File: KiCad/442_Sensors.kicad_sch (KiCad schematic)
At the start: 9 parts, among them U4 MS560702BA03-50, U5 BMI088, U6 SAM-M10Q

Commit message: fixed a couple issues
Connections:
- net +3V3: no longer U4.4 (~{CSB})
- net GND: now also U4.4 (~{CSB})
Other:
- moved on the sheet: C20
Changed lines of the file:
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@@
+	)
+	(junction
+		(at 88.9 99.06)
+		(diameter 0)
+		(color 0 0 0 0)
 	)
 	(junction
@@
 	(wire
 		(pts
-			(xy 133.35 96.52) (xy 137.16 96.52)
+			(xy 133.35 97.79) (xy 133.35 96.52)
 		)
 		(stroke
@@
 	(wire
 		(pts
-			(xy 77.47 96.52) (xy 91.44 96.52)
-		)
-		(stroke
-			(width 0)
-			(type default)
-		)
-	)
-	(wire
-		(pts
 			(xy 194.31 81.28) (xy 200.66 81.28)
 		)
@@
 	(wire
 		(pts
-			(xy 80.01 99.06) (xy 91.44 99.06)
+			(xy 88.9 99.06) (xy 91.44 99.06)
+		)
+		(stroke
+			(width 0)
+			(type default)
+		)
+	)
+	(wire
+		(pts
+			(xy 80.01 99.06) (xy 88.9 99.06)
 		)
 		(stroke
@@
 	(wire
 		(pts
+			(xy 88.9 96.52) (xy 88.9 99.06)
+		)
+		(stroke
+			(width 0)
+			(type default)
+		)
+	)
+	(wire
+		(pts
 			(xy 113.03 46.99) (xy 95.25 46.99)
 		)
@@
 	(wire
 		(pts
+			(xy 91.44 96.52) (xy 88.9 96.52)
+		)
+		(stroke
+			(width 0)
+			(type default)
+		)
+	)
+	(wire
+		(pts
 			(xy 194.31 78.74) (xy 200.66 78.74)
 		)
@@
 		(pts
 			(xy 121.92 106.68) (xy 123.19 106.68)
+		)
+		(stroke
+			(width 0)
+			(type default)
+		)
+	)
+	(wire
+		(pts
+			(xy 133.35 95.25) (xy 133.35 96.52)
 		)
 		(stroke
@@
 	(symbol
 		(lib_id "power:GND")
-		(at 133.35 101.6 0)
+		(at 133.35 102.87 0)
 		(unit 1)
 		(exclude_from_sim no)
@@
 		(fields_autoplaced yes)
 		(property "Reference" "#PWR051"
+			(at 133.35 109.22 0)
+			(effects
+				(font
+					(size 1.27 1.27)
+				)
+				(hide yes)
+			)
+		)
+		(property "Value" "GND"
 			(at 133.35 107.95 0)
 			(effects
@@
 					(size 1.27 1.27)
 				)
-				(hide yes)
-			)
-		)
-		(property "Value" "GND"
-			(at 133.35 106.68 0)
-			(effects
-				(font
-					(size 1.27 1.27)
-				)
 			)
 		)
 		(property "Footprint" ""
-			(at 133.35 101.6 0)
+			(at 133.35 102.87 0)
 			(effects
 				(font
@@
 		)
 		(property "Datasheet" ""
-			(at 133.35 101.6 0)
+			(at 133.35 102.87 0)
 			(effects
 				(font
@@
 		)
 		(property "Description" "Power symbol creates a global label with name \"GND\" , ground"
-			(at 133.35 101.6 0)
+			(at 133.35 102.87 0)
 			(effects
 				(font
@@
 	(symbol
 		(lib_id "power:+3V3")
-		(at 137.16 96.52 270)
+		(at 133.35 95.25 0)
 		(unit 1)
 		(exclude_from_sim no)
@@
 		(fields_autoplaced yes)
 		(property "Reference" "#PWR063"
-			(at 133.35 96.52 0)
+			(at 133.35 99.06 0)
 			(effects
 				(font
@@
 		)
 		(property "Value" "+3V3"
-			(at 140.97 96.5199 90)
+			(at 135.89 93.9799 0)
 			(effects
 				(font
@@
 		)
 		(property "Footprint" ""
-			(at 137.16 96.52 0)
+			(at 133.35 95.25 0)
 			(effects
 				(font
@@
 		)
 		(property "Datasheet" ""
-			(at 137.16 96.52 0)
+			(at 133.35 95.25 0)
 			(effects
 				(font
@@
 		)
 		(property "Description" "Power symbol creates a global label with name \"+3V3\""
-			(at 137.16 96.52 0)
+			(at 133.35 95.25 0)
 			(effects
 				(font
@@
 	(symbol
 		(lib_id "power:+3V3")
-		(at 77.47 96.52 90)
-		(unit 1)
-		(exclude_from_sim no)
-		(in_bom yes)
-		(on_board yes)
-		(dnp no)
-		(fields_autoplaced yes)
-		(property "Reference" "#PWR064"
-			(at 81.28 96.52 0)
-			(effects
-				(font
-					(size 1.27 1.27)
-				)
-				(hide yes)
-			)
-		)
-		(property "Value" "+3V3"
-			(at 73.66 96.5199 90)
-			(effects
-				(font
-					(size 1.27 1.27)
-				)
-				(justify left)
-			)
-		)
-		(property "Footprint" ""
-			(at 77.47 96.52 0)
-			(effects
-				(font
-					(size 1.27 1.27)
-				)
-				(hide yes)
-			)
-		)
-		(property "Datasheet" ""
-			(at 77.47 96.52 0)
-			(effects
-				(font
-					(size 1.27 1.27)
-				)
-				(hide yes)
-			)
-		)
-		(property "Description" "Power symbol creates a global label with name \"+3V3\""
-			(at 77.47 96.52 0)
-			(effects
-				(font
-					(size 1.27 1.27)
-				)
-				(hide yes)
-			)
-		)
-		(pin "1"
-		)
-		(instances
-			(project "Senior Project"
-				(path "/16f8cce7-467e-4342-b55a-00af81cd6f69/c3ab4c5a-4cab-469f-8c3a-b4c939a78ff3"
-					(reference "#PWR064")
-					(unit 1)
-				)
-			)
-		)
-	)
-	(symbol
-		(lib_id "power:+3V3")
 		(at 113.03 46.99 0)
 		(unit 1)
@@
 	(symbol
 		(lib_id "Device:C_Small")
-		(at 133.35 99.06 0)
+		(at 133.35 100.33 0)
 		(unit 1)
 		(exclude_from_sim no)
@@
 		(fields_autoplaced yes)
 		(property "Reference" "C20"
-			(at 135.89 97.7962 0)
+			(at 135.89 99.0662 0)
 			(effects
 				(font
@@
 		)
 		(property "Value" "100nF"
-			(at 135.89 100.3362 0)
+			(at 135.89 101.6062 0)
 			(effects
 				(font
@@
 		)
 		(property "Footprint" "Capacitor_SMD:C_0402_1005Metric"
-			(at 133.35 99.06 0)
+			(at 133.35 100.33 0)
 			(effects
 				(font
@@
 		)
 		(property "Datasheet" "~"
-			(at 133.35 99.06 0)
+			(at 133.35 100.33 0)
 			(effects
 				(font
@@
 		)
 		(property "Description" "Unpolarized capacitor, small symbol"
-			(at 133.35 99.06 0)
+			(at 133.35 100.33 0)
 			(effects
 				(font
@@
 		)
 		(property "LCSC" "C1525"
-			(at 133.35 99.06 0)
-			(effects
-				(font
+			(at 133.35 100.33 0)
+			(effects
+				(font

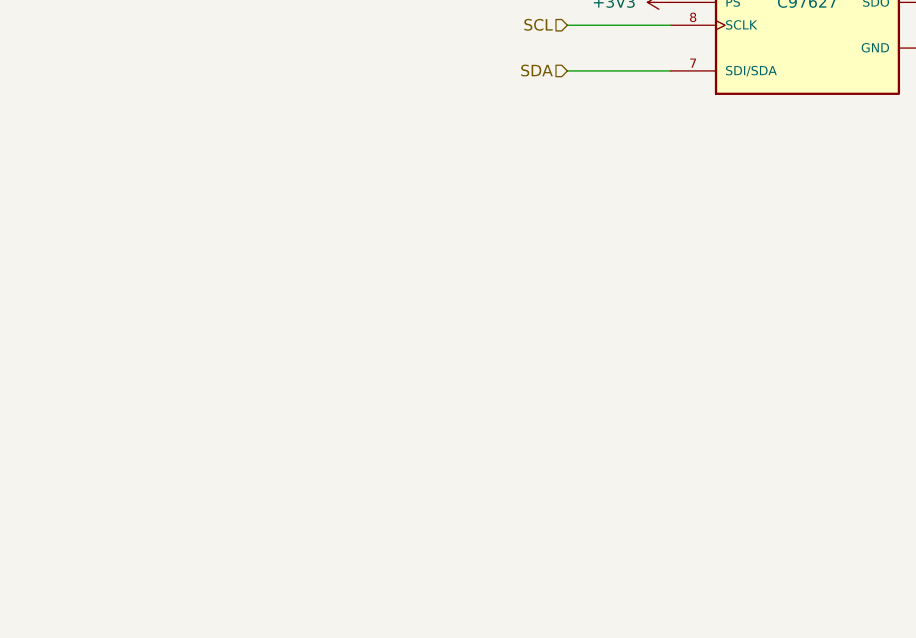
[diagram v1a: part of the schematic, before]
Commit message: add spot for high G accelerometer
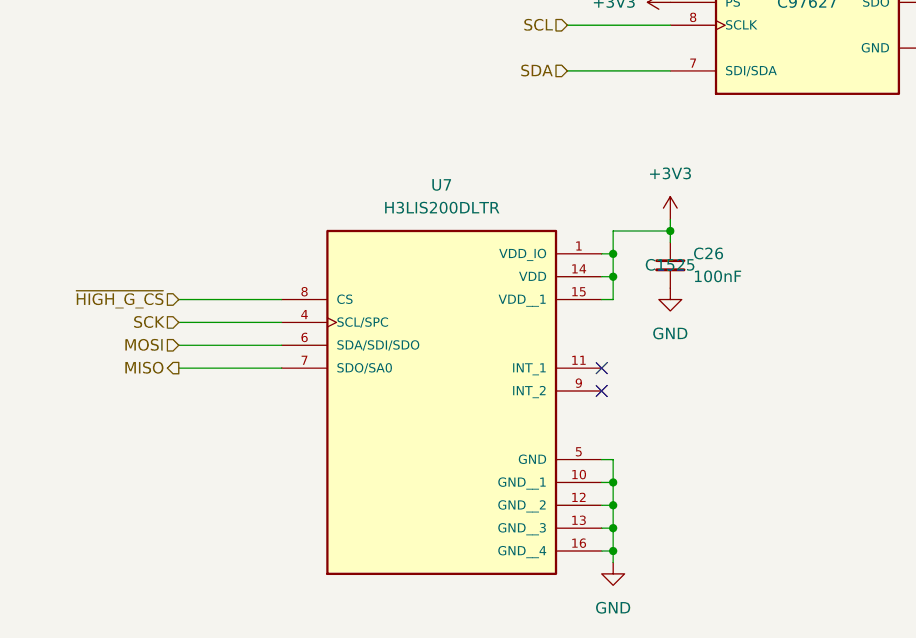
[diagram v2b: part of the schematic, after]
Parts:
- added C26: 100nF, Capacitor_SMD:C_0402_1005Metric, symbol Device:C_Small
- added U7: H3LIS200DLTR, asdt-5:PQFN50P300X300X100-16N, symbol H3LIS200DLTR:H3LIS200DLTR
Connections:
- net +3V3: now also C26.1, U7.1 (VDD_IO), U7.14 (VDD), U7.15 (VDD__1)
- net GND: now also C26.2, U7.10 (GND__1), U7.12 (GND__2), U7.13 (GND__3), U7.16 (GND__4), U7.5 (GND)
- net MISO: now also U7.7 (SDO/SA0)
- net MOSI: now also U7.6 (SDA/SDI/SDO)
- net SCK: now also U7.4 (SCL/SPC)
- new net ~{HIGH_G_CS}: U7.8 (CS)
- no-connect marks 10 -> 12
